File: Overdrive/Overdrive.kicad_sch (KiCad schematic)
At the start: 44 parts, among them J2 Barrel_Jack_Switch, J3 Stereo In, J4 Mono Out, Q1 2N2222, Q2 2N2222, SW1 Footswitch, U1 RC4558

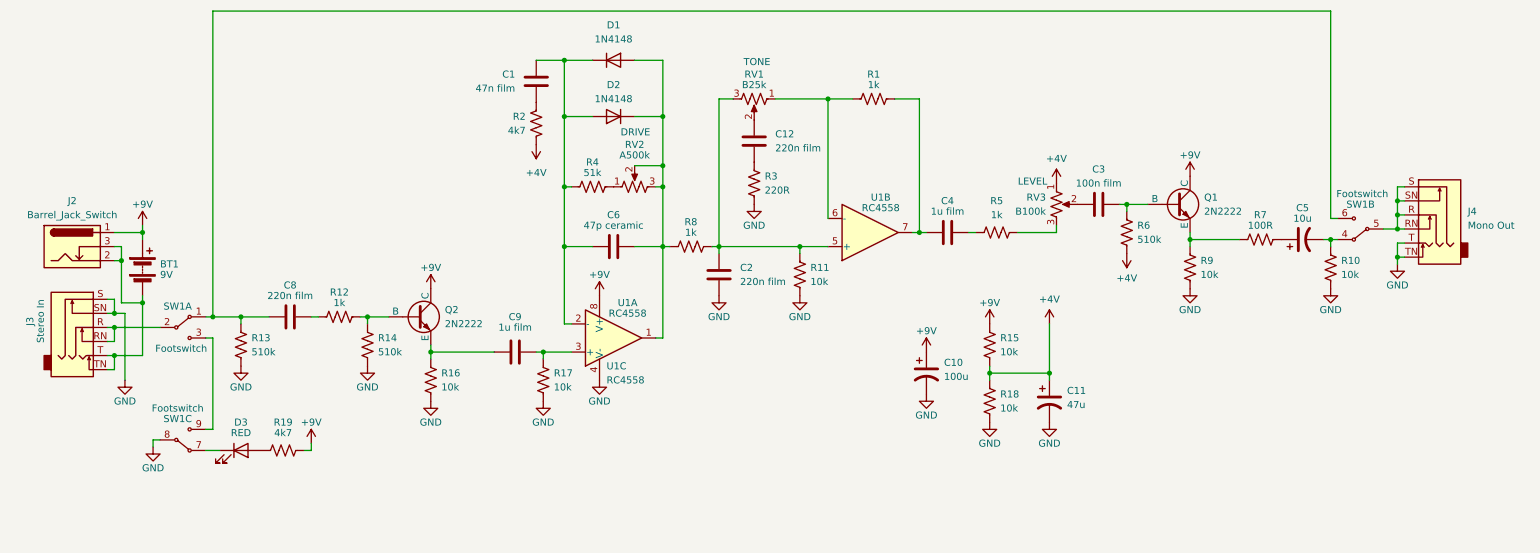
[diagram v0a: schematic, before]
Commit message: Fixed schematic errors
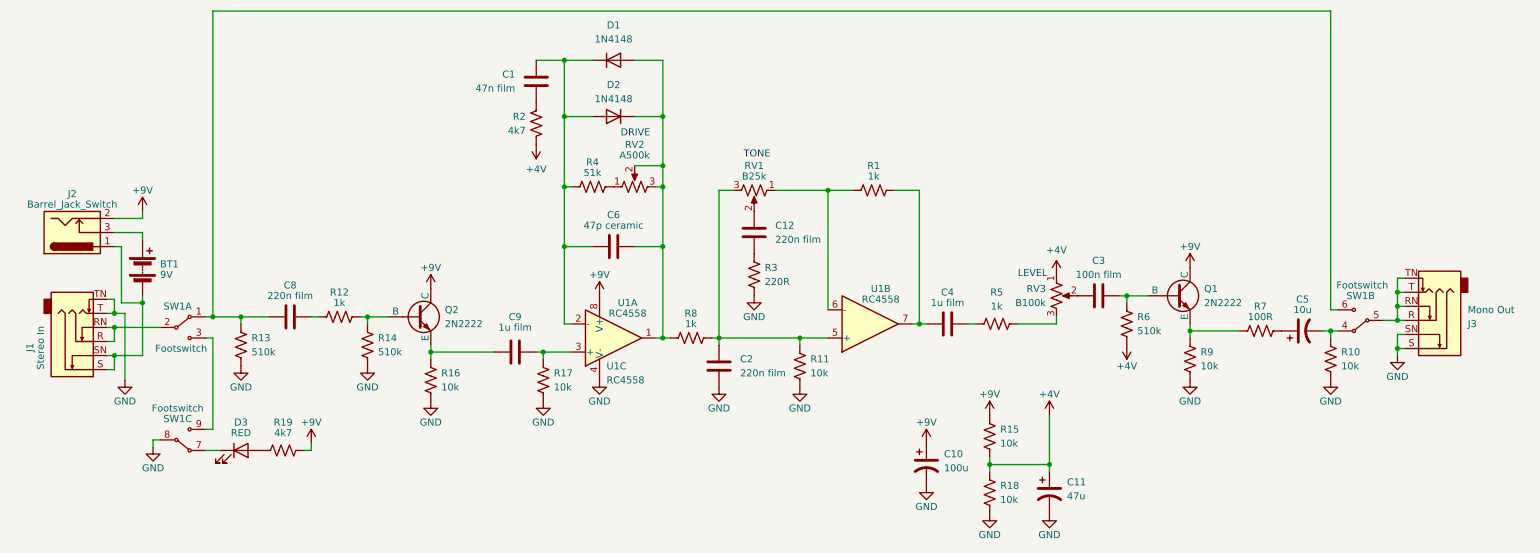
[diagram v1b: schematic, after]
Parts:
- removed J4: Mono Out, Connector_Audio:Jack_6.35mm_Neutrik_NRJ6HM-1-AU_Horizontal, symbol Connector_Audio:AudioJack3_Switch
- added J1: Stereo In, Connector_Audio:Jack_6.35mm_Neutrik_NRJ6HM-1-AU_Horizontal, symbol Connector_Audio:AudioJack3_Switch
- J3: value Stereo In -> Mono Out
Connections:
- net +9V: now also J2.2; no longer BT1.1 (+), J2.1
- net GND: now also J1.T, J1.TN
- net at J3.R, J3.RN: now also J3.T, J3.TN, SW1.5; no longer SW1.2
- new net: J1.R, J1.RN, SW1.2
- new net: BT1.2 (-), J1.S, J1.SN, J2.1
- new net: BT1.1 (+), J2.3
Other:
- moved on the sheet: C10, C11, C12, C2, C3, C4, C5, J2, Q1, R1, R10, R11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

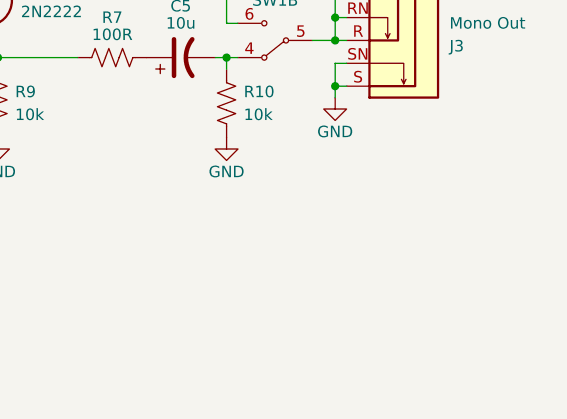
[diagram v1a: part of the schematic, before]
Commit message: Fixed PCB errors and added logos
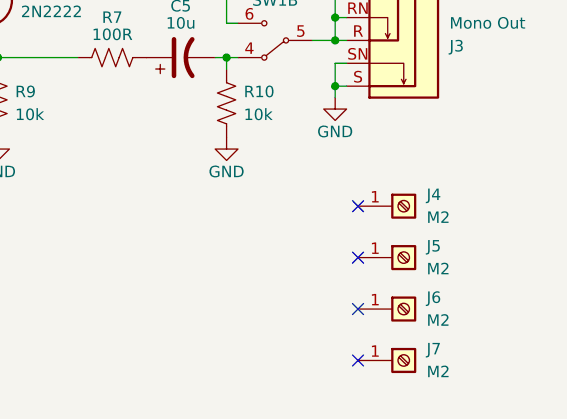
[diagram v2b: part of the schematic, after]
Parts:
- added J4, J5, J6, J7: M2, MountingHole:MountingHole_2.2mm_M2_DIN965_Pad, symbol Connector:Screw_Terminal_01x01
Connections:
- no-connect marks 0 -> 4
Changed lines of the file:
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@@
   (junction (at 160.655 78.105) (diameter 0) (color 0 0 0 0)
   )
+  (no_connect (at 266.065 137.16))
+  (no_connect (at 266.065 125.73))
+  (no_connect (at 266.065 120.015))
+  (no_connect (at 266.065 131.445))
   (wire (pts (xy 251.46 99.695) (xy 252.73 99.695))
     (stroke (width 0) (type default))
@@
     )
   )
+  (symbol (lib_id "Connector:Screw_Terminal_01x01") (at 271.145 120.015 0) (unit 1)
+    (in_bom yes) (on_board yes) (dnp no) (fields_autoplaced)
+    (property "Reference" "J4" (at 273.685 118.7449 0)
+      (effects (font (size 1.27 1.27)) (justify left))
+    )
+    (property "Value" "M2" (at 273.685 121.2849 0)
+      (effects (font (size 1.27 1.27)) (justify left))
+    )
+    (property "Footprint" "MountingHole:MountingHole_2.2mm_M2_DIN965_Pad" (at 271.145 120.015 0)
+      (effects (font (size 1.27 1.27)) hide)
+    )
+    (property "Datasheet" "~" (at 271.145 120.015 0)
+      (effects (font (size 1.27 1.27)) hide)
+    )
+    (pin "1")
+    (instances
+      (project "Overdrive"
+        (path "/fe0ef748-c0e2-4e36-9675-7bcda993069a"
+          (reference "J4") (unit 1)
+        )
+      )
+    )
+  )
   (symbol (lib_id "Device:C_Polarized_US") (at 200.66 132.715 0) (unit 1)
     (in_bom yes) (on_board yes) (dnp no) (fields_autoplaced)
@@
         (path "/fe0ef748-c0e2-4e36-9675-7bcda993069a"
           (reference "C11") (unit 1)
+        )
+      )
+    )
+  )
+  (symbol (lib_id "Connector:Screw_Terminal_01x01") (at 271.145 125.73 0) (unit 1)
+    (in_bom yes) (on_board yes) (dnp no) (fields_autoplaced)
+    (property "Reference" "J5" (at 273.685 124.4599 0)
+      (effects (font (size 1.27 1.27)) (justify left))
+    )
+    (property "Value" "M2" (at 273.685 126.9999 0)
+      (effects (font (size 1.27 1.27)) (justify left))
+    )
+    (property "Footprint" "MountingHole:MountingHole_2.2mm_M2_DIN965_Pad" (at 271.145 125.73 0)
+      (effects (font (size 1.27 1.27)) hide)
+    )
+    (property "Datasheet" "~" (at 271.145 125.73 0)
+      (effects (font (size 1.27 1.27)) hide)
+    )
+    (pin "1")
+    (instances
+      (project "Overdrive"
+        (path "/fe0ef748-c0e2-4e36-9675-7bcda993069a"
+          (reference "J5") (unit 1)
         )
       )
@@
     )
   )
+  (symbol (lib_id "Connector:Screw_Terminal_01x01") (at 271.145 131.445 0) (unit 1)
+    (in_bom yes) (on_board yes) (dnp no) (fields_autoplaced)
+    (property "Reference" "J6" (at 273.685 130.1749 0)
+      (effects (font (size 1.27 1.27)) (justify left))
+    )
+    (property "Value" "M2" (at 273.685 132.7149 0)
+      (effects (font (size 1.27 1.27)) (justify left))
+    )
+    (property "Footprint" "MountingHole:MountingHole_2.2mm_M2_DIN965_Pad" (at 271.145 131.445 0)
+      (effects (font (size 1.27 1.27)) hide)
+    )
+    (property "Datasheet" "~" (at 271.145 131.445 0)
+      (effects (font (size 1.27 1.27)) hide)
+    )
+    (pin "1")
+    (instances
+      (project "Overdrive"
+        (path "/fe0ef748-c0e2-4e36-9675-7bcda993069a"
+          (reference "J6") (unit 1)
+        )
+      )
+    )
+  )
   (symbol (lib_id "power:GND") (at 155.575 113.665 0) (unit 1)
     (in_bom yes) (on_board yes) (dnp no)
@@
         )
       )
+    )
+  )
+  (symbol (lib_id "Connector:Screw_Terminal_01x01") (at 271.145 137.16 0) (unit 1)
+    (in_bom yes) (on_board yes) (dnp no) (fields_autoplaced)
+    (property "Reference" "J7" (at 273.685 135.8899 0)
+      (effects (font (size 1.27 1.27)) (justify left))
+    )
+    (property "Value" "M2" (at 273.685 138.4299 0)
+      (effects (font (size 1.27 1.27)) (justify left))
+    )
+    (property "Footprint" "MountingHole:MountingHole_2.2mm_M2_DIN965_Pad" (at 271.145 137.16 0)
+      (effects (font (size 1.27 1.27)) hide)
+    )
+    (property "Datasheet" "~" (at 271.145 137.16 0)
+      (effects (font (size 1.27 1.27)) hide)
+    )
+    (pin "1")
+    (instances
+      (project "Overdrive"
+        (path "/fe0ef748-c0e2-4e36-9675-7bcda993069a"
+          (reference "J7") (unit 1)
+        )
+      )

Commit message: Redesigned board to fit 125B case
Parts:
- J4, J5, J6, J7: footprint MountingHole:MountingHole_2.2mm_M2_DIN965_Pad -> MountingHole:MountingHole_3.2mm_M3_DIN965_Pad
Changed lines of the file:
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@@
       (effects (font (size 1.27 1.27)) (justify left))
     )
-    (property "Footprint" "MountingHole:MountingHole_2.2mm_M2_DIN965_Pad" (at 271.145 120.015 0)
+    (property "Footprint" "MountingHole:MountingHole_3.2mm_M3_DIN965_Pad" (at 271.145 120.015 0)
       (effects (font (size 1.27 1.27)) hide)
     )
@@
       (effects (font (size 1.27 1.27)) (justify left))
     )
-    (property "Footprint" "MountingHole:MountingHole_2.2mm_M2_DIN965_Pad" (at 271.145 125.73 0)
+    (property "Footprint" "MountingHole:MountingHole_3.2mm_M3_DIN965_Pad" (at 271.145 125.73 0)
       (effects (font (size 1.27 1.27)) hide)
     )
@@
       (effects (font (size 1.27 1.27)) (justify left))
     )
-    (property "Footprint" "MountingHole:MountingHole_2.2mm_M2_DIN965_Pad" (at 271.145 131.445 0)
+    (property "Footprint" "MountingHole:MountingHole_3.2mm_M3_DIN965_Pad" (at 271.145 131.445 0)
       (effects (font (size 1.27 1.27)) hide)
     )
@@
       (effects (font (size 1.27 1.27)) (justify left))
     )
-    (property "Footprint" "MountingHole:MountingHole_2.2mm_M2_DIN965_Pad" (at 271.145 137.16 0)
-      (effects (font (size 1.27 1.27)) hide)
-    )
+    (property "Footprint" "MountingHole:MountingHole_3.2mm_M3_DIN965_Pad" (at 271.145 137.16 0)
+      (effects (font (size 1.27 1.27)) hide)
+    )

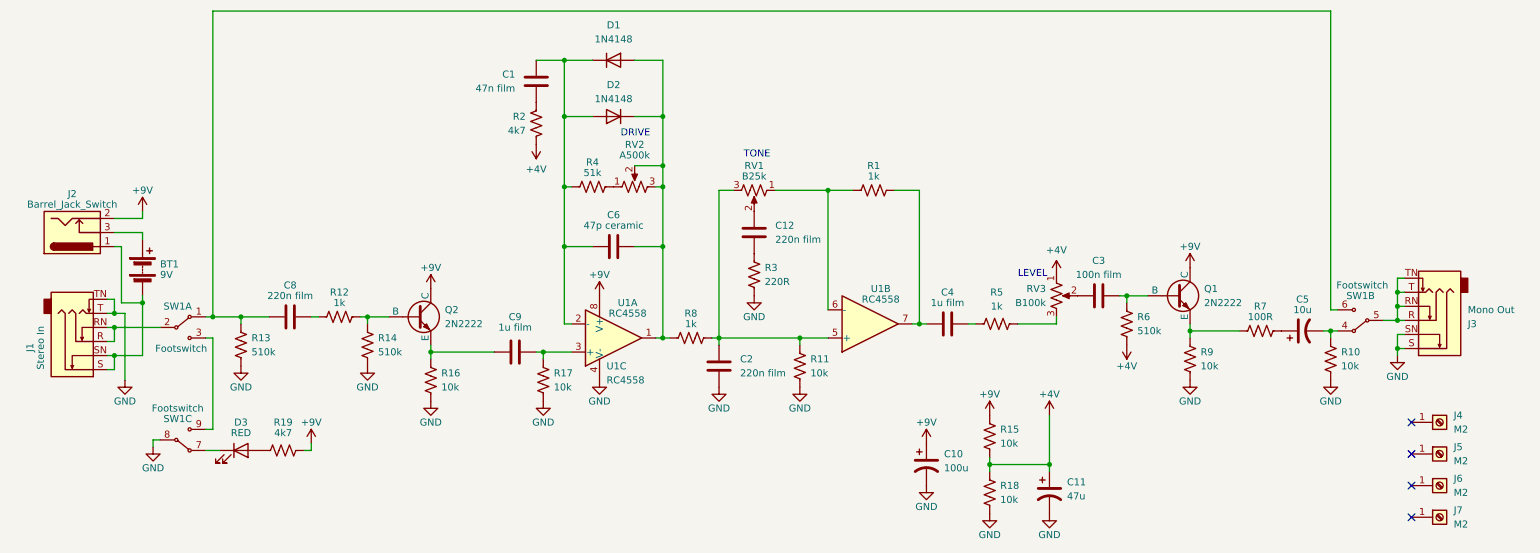
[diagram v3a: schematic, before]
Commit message: error correction in switches
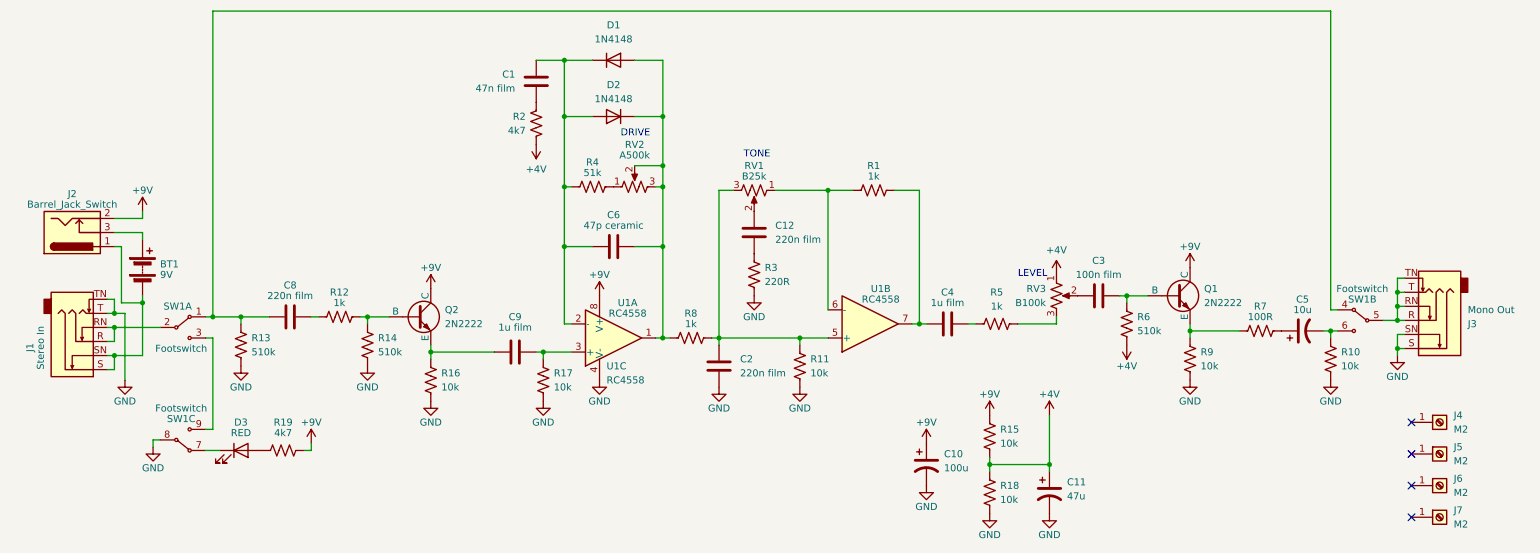
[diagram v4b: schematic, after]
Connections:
- net at C8.1, R13.1, SW1.1: now also SW1.4; no longer SW1.6
- net at C5.2, R10.1: now also SW1.6; no longer SW1.4
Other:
- moved on the sheet: SW1B
